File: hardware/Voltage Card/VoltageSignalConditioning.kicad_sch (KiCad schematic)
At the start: 4 parts

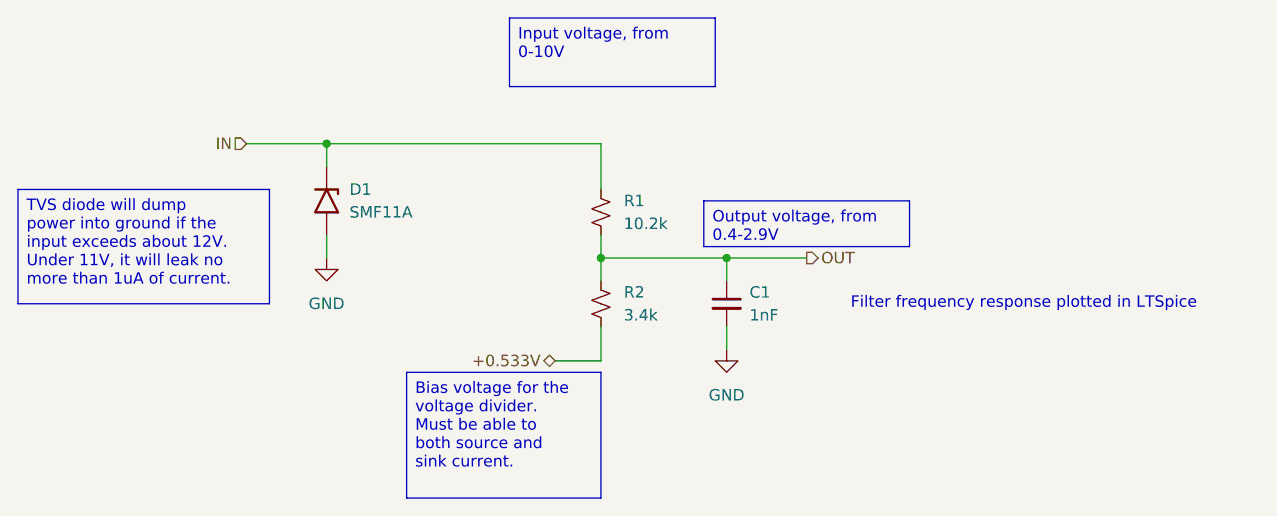
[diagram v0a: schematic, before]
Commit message: Route more of main unit, start on KiBot CI job
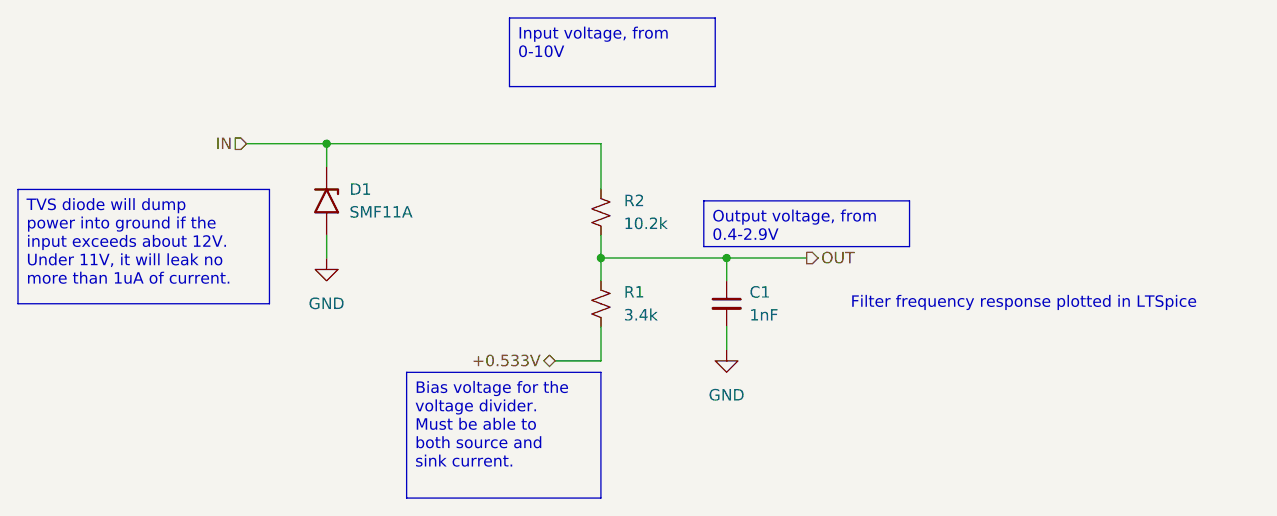
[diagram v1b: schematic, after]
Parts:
- renumbered R2 to R1, R1 to R2
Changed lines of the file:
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@@
 		(dnp no)
 		(fields_autoplaced yes)
-		(property "Reference" "R2"
+		(property "Reference" "R1"
 			(at 101.6 57.1499 0)
 			(effects
@@
 			)
 		)
-		(property "Description" "Resistor 3.4k 0.1% 0.1W 0603"
+		(property "Description" "Resistor, small US symbol"
 			(at 99.06 58.42 0)
 			(effects
@@
 			(project "HackerDAQ Voltage Card"
 				(path "/af2d881c-6553-449d-9093-6deb41497bdc/01e32aea-7249-45cf-93de-969f26bb59ad"
-					(reference "R12")
+					(reference "R11")
 					(unit 1)
 				)
 				(path "/af2d881c-6553-449d-9093-6deb41497bdc/19e2c91d-acca-425e-b032-18a02789338f"
-					(reference "R2")
+					(reference "R1")
 					(unit 1)
 				)
 				(path "/af2d881c-6553-449d-9093-6deb41497bdc/364da5c8-794e-452e-ba60-34e27f9ef1d7"
-					(reference "R14")
+					(reference "R13")
 					(unit 1)
 				)
 				(path "/af2d881c-6553-449d-9093-6deb41497bdc/52e0dd60-70d7-4a7b-bed8-3d2caece0327"
-					(reference "R6")
+					(reference "R5")
 					(unit 1)
 				)
 				(path "/af2d881c-6553-449d-9093-6deb41497bdc/5accc0a3-8603-4541-8753-addba01167d7"
-					(reference "R4")
+					(reference "R3")
 					(unit 1)
 				)
 				(path "/af2d881c-6553-449d-9093-6deb41497bdc/7df301f9-3e32-4f53-8264-a6bdc7a65263"
-					(reference "R16")
+					(reference "R15")
 					(unit 1)
 				)
 				(path "/af2d881c-6553-449d-9093-6deb41497bdc/8e661f41-f558-42a9-afea-ef14e2a58eed"
-					(reference "R8")
+					(reference "R7")
 					(unit 1)
 				)
 				(path "/af2d881c-6553-449d-9093-6deb41497bdc/a21689b1-0d98-48c2-bd74-0bdf8e3941e7"
-					(reference "R10")
+					(reference "R9")
 					(unit 1)
 				)
@@
 		(dnp no)
 		(fields_autoplaced yes)
-		(property "Reference" "R1"
+		(property "Reference" "R2"
 			(at 101.6 46.9899 0)
 			(effects
@@
 			)
 		)
-		(property "Description" "Resistor 10.2k 0.1% 0.1W 0603"
+		(property "Description" "Resistor, small US symbol"
 			(at 99.06 48.26 0)
 			(effects
@@
 			(project "HackerDAQ Voltage Card"
 				(path "/af2d881c-6553-449d-9093-6deb41497bdc/01e32aea-7249-45cf-93de-969f26bb59ad"
-					(reference "R11")
+					(reference "R12")
 					(unit 1)
 				)
 				(path "/af2d881c-6553-449d-9093-6deb41497bdc/19e2c91d-acca-425e-b032-18a02789338f"
-					(reference "R1")
+					(reference "R2")
 					(unit 1)
 				)
 				(path "/af2d881c-6553-449d-9093-6deb41497bdc/364da5c8-794e-452e-ba60-34e27f9ef1d7"
-					(reference "R13")
+					(reference "R14")
 					(unit 1)
 				)
 				(path "/af2d881c-6553-449d-9093-6deb41497bdc/52e0dd60-70d7-4a7b-bed8-3d2caece0327"
-					(reference "R5")
+					(reference "R6")
 					(unit 1)
 				)
 				(path "/af2d881c-6553-449d-9093-6deb41497bdc/5accc0a3-8603-4541-8753-addba01167d7"
-					(reference "R3")
+					(reference "R4")
 					(unit 1)
 				)
 				(path "/af2d881c-6553-449d-9093-6deb41497bdc/7df301f9-3e32-4f53-8264-a6bdc7a65263"
-					(reference "R15")
+					(reference "R16")
 					(unit 1)
 				)
 				(path "/af2d881c-6553-449d-9093-6deb41497bdc/8e661f41-f558-42a9-afea-ef14e2a58eed"
-					(reference "R7")
+					(reference "R8")
 					(unit 1)
 				)
 				(path "/af2d881c-6553-449d-9093-6deb41497bdc/a21689b1-0d98-48c2-bd74-0bdf8e3941e7"
-					(reference "R9")
+					(reference "R10")
 					(unit 1)
 				)
@@
 			)
 		)
-		(property "Datasheet" "https://www.littelfuse.com/assetdocs/tvs-diodes-smf-datasheet?assetguid=7eb8a5b6-bdd0-4561-8f19-0c3cc6f9b2af"
+		(property "Datasheet" "https://www.vishay.com/doc?85881"
 			(at 68.58 45.72 0)
 			(effects
@@
 			)
 		)
-		(property "Description" "200W unidirectional TVS diode, Vr=11V, Vbreakdown=12.2V"
+		(property "Description" "200W unidirectional Transil Transient Voltage Suppressor, 11Vrwm, SMF"
 			(at 68.58 46.99 0)
 			(effects
@@
 			)
 		)
-		(property "Description" "Ceramic Cap 1nF 5% 50V, C0G, 0603"
+		(property "Description" "Unpolarized capacitor, small symbol"
 			(at 113.03 58.42 0)
 			(effects

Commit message: Add Main Unit to CI build as well
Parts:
- C1: LibRef (none) -> CL10B102KC8WPNC
- R1: LibRef (none) -> RT0603BRD073K4L
- R2: LibRef (none) -> RT0603BRD0710K2L
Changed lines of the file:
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@@
+			)
+		)
+		(property "LibRef" "RT0603BRD073K4L"
+			(at 99.06 58.42 0)
+			(effects
+				(font
+					(size 1.27 1.27)
+				)
+				(hide yes)
 			)
 		)
@@
 			)
 		)
+		(property "LibRef" "RT0603BRD0710K2L"
+			(at 99.06 48.26 0)
+			(effects
+				(font
+					(size 1.27 1.27)
+				)
+				(hide yes)
+			)
+		)
 		(pin "2"
 		)
@@
 			(at 113.03 58.42 0)
 			(effects
+				(font
+					(size 1.27 1.27)
+				)
+				(hide yes)
+			)
+		)
+		(property "LibRef" "CL10B102KC8WPNC"
+			(at 113.03 58.42 0)
+			(effects
